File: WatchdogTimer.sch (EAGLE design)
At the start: 20 parts, among them IC1 LM555D, Q2 MOSFET-NCHANNELSMD

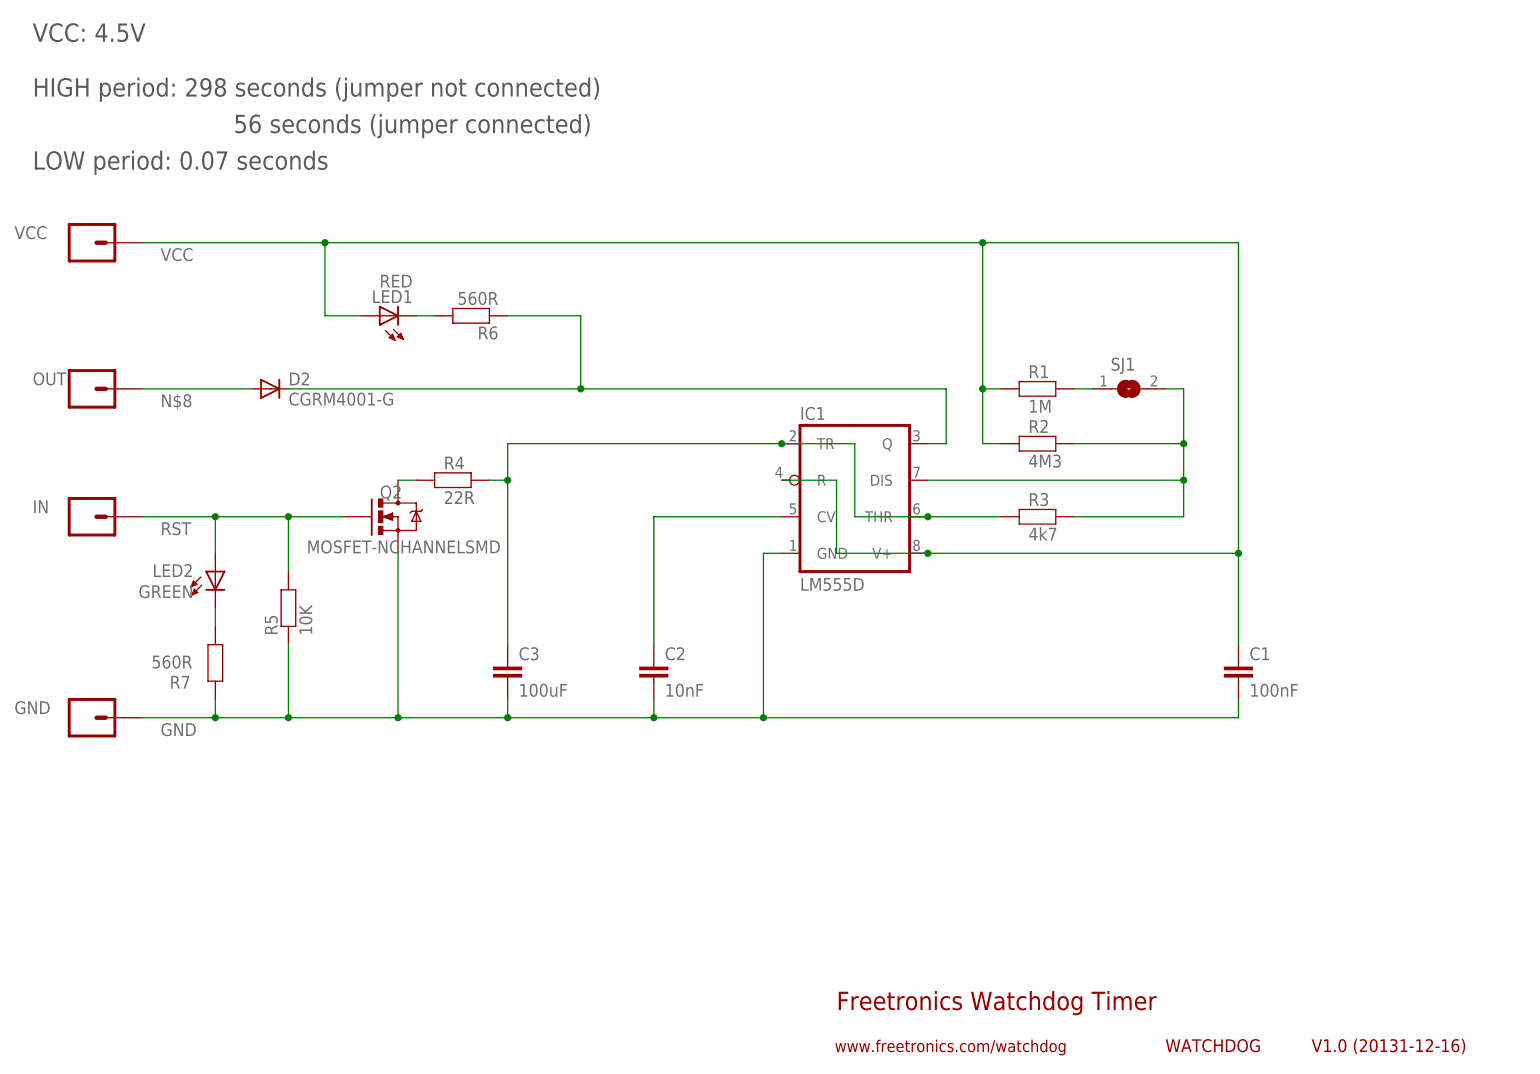
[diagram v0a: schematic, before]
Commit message: Replaced main timing cap with 1206 tantalum for size reasons Updates to routing and labels
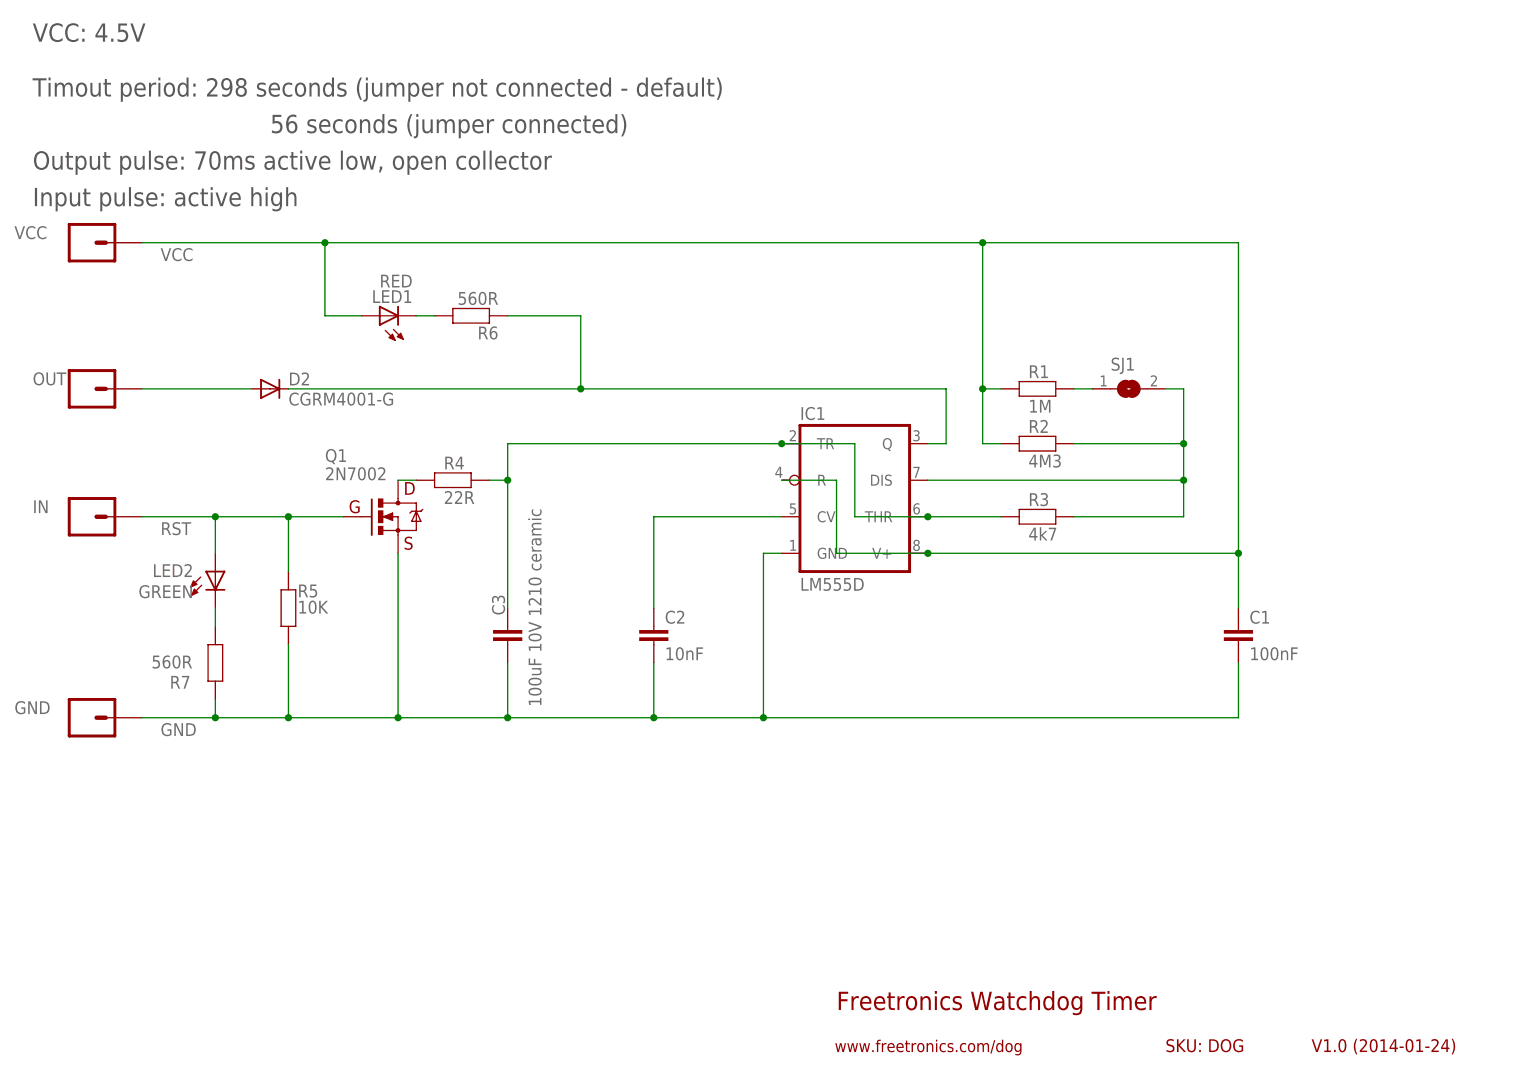
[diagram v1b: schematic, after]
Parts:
- C3: value 100uF -> 100uF 10V 1210 ceramic; device freetronics-master-v1:CAP0603 -> freetronics-jon:C-EUC1210
- Q1: value MOSFET-NCHANNELSMD -> 2N7002
- renumbered Q2 to Q1
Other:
- note added: "D"
- note added: "G"
- note added: "Input pulse: active high"
- note added: "Output pulse: 70ms active low, open collector"
- note added: "S"
- note added: "SKU: DOG"
- note added: "Timout period: 298 seconds (jumper not connected - default)"
- note added: "V1.0 (2014-01-24)"
- note added: "www.freetronics.com/dog"
- note removed: "HIGH period: 298 seconds (jumper not connected)"
- note removed: "LOW period: 0.07 seconds"
- note removed: "V1.0 (20131-12-16)"
- note removed: "WATCHDOG"
- note removed: "www.freetronics.com/watchdog"
- moved on the sheet: C1, C2, C3
